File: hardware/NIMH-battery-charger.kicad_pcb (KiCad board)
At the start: 2 copper layers, 66 x 79.8 mm, 27 parts, among them J1 Conn_01x03_Pin, J3 Conn_01x01_Pin, J4 Conn_01x01_Pin, J5 Conn_01x01_Pin, J6 Conn_01x01_Pin, J7 USB_C_Receptacle_PowerOnly_6P, U1 CH32V003f4u6

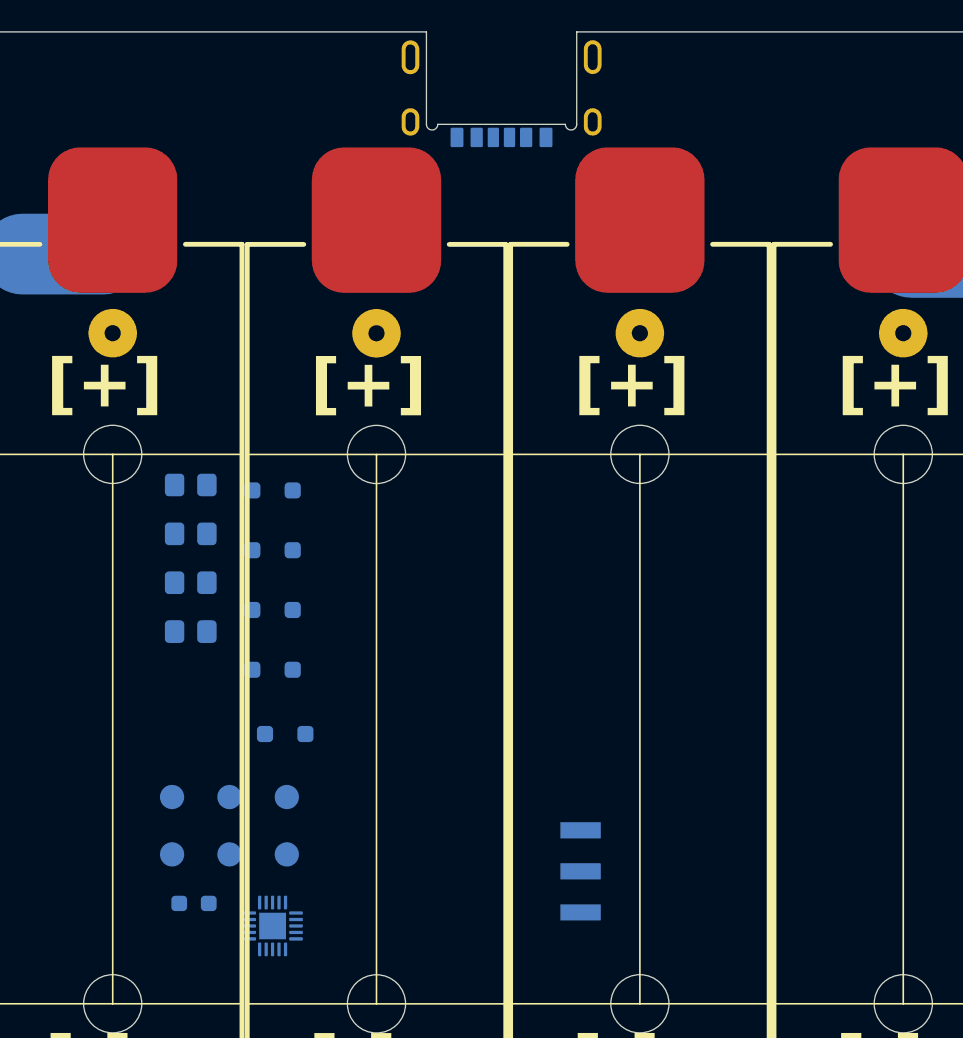
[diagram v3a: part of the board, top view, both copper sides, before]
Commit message: Add leds
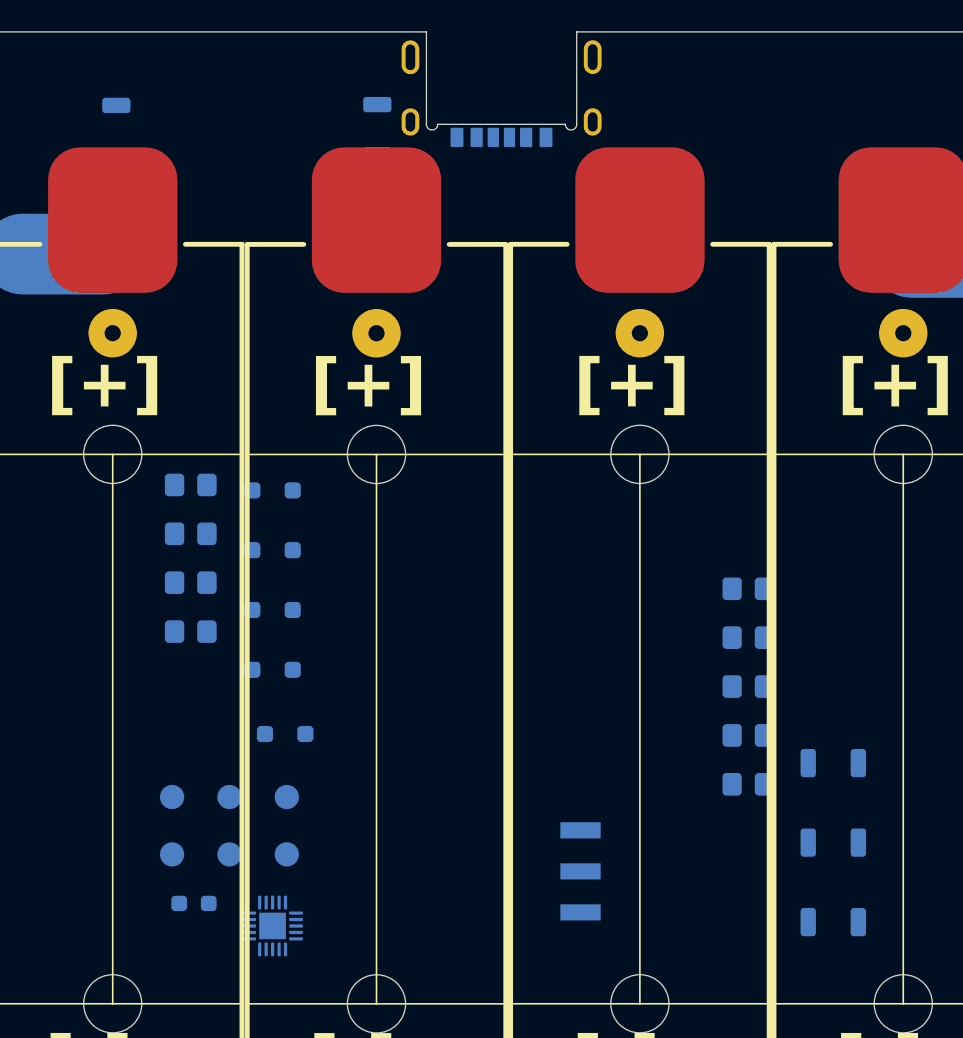
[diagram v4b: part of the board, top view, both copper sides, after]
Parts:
- added D10: LED, PCM_LED_SMD_AKL:LED_1206_3216Metric_ReverseMount_Hole1.8x2.4mm, B.Cu at (157.7, 99.1)
- added D5: LED, PCM_LED_SMD_AKL:LED_1206_3216Metric_ReverseMount_Hole1.8x2.4mm, B.Cu at (113.3, 50.1)
- added D6: LED, PCM_LED_SMD_AKL:LED_1206_3216Metric_ReverseMount_Hole1.8x2.4mm, B.Cu at (129.4, 50.1)
- added D7: LED, PCM_LED_SMD_AKL:LED_1206_3216Metric_ReverseMount_Hole1.8x2.4mm, B.Cu at (157.7, 89.3)
- added D8: LED, PCM_LED_SMD_AKL:LED_1206_3216Metric_ReverseMount_Hole1.8x2.4mm, B.Cu at (157.7, 94.2)
- added R10: 220R, PCM_Resistor_SMD_AKL:R_0805_2012Metric_Pad1.20x1.40mm_HandSolder, B.Cu at (152.4, 90.6)
- added R6: 220R, PCM_Resistor_SMD_AKL:R_0805_2012Metric_Pad1.20x1.40mm_HandSolder, B.Cu at (152.4, 78.5)
- added R7: 220R, PCM_Resistor_SMD_AKL:R_0805_2012Metric_Pad1.20x1.40mm_HandSolder, B.Cu at (152.4, 81.5)
- added R8: 220R, PCM_Resistor_SMD_AKL:R_0805_2012Metric_Pad1.20x1.40mm_HandSolder, B.Cu at (152.4, 84.6)
- added R9: 220R, PCM_Resistor_SMD_AKL:R_0805_2012Metric_Pad1.20x1.40mm_HandSolder, B.Cu at (152.4, 87.6)

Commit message: Moving Leds
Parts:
- moved D7 40.0 mm to (137.2, 54.9), turned to 90 degrees
- moved R6 0.09 mm to (152.5, 78.5)
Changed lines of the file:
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@@
 	(footprint "PCM_LED_SMD_AKL:LED_1206_3216Metric_ReverseMount_Hole1.8x2.4mm"
 		(layer "B.Cu")
-		(at 157.669668 89.3 180)
+		(at 137.25 54.85 90)
 		(descr "LED SMD 1206 (3216 Metric), reverse mount, square (rectangular) end terminal, IPC_7351 nominal, (Body size source: http://www.tortai-tech.com/upload/download/2011102023233369053.pdf), generated with kicad-footprint-generator")
 		(tags "diode reverse")
 		(property "Reference" "D7"
-			(at 0 2.545 0)
+			(at 0 2.545 90)
 			(layer "B.SilkS")
 			(effects
@@
 		)
 		(property "Value" "LED"
-			(at 0 -2.145 0)
+			(at 0 -2.145 90)
 			(layer "B.Fab")
 			(hide yes)
@@
 		)
 		(property "Footprint" "PCM_LED_SMD_AKL:LED_1206_3216Metric_ReverseMount_Hole1.8x2.4mm"
-			(at 0 0 0)
+			(at 0 0 90)
 			(layer "B.Fab")
 			(hide yes)
@@
 		)
 		(property "Datasheet" ""
-			(at 0 0 0)
+			(at 0 0 90)
 			(layer "B.Fab")
 			(hide yes)
@@
 		)
 		(property "Description" "Light emitting diode"
-			(at 0 0 0)
+			(at 0 0 90)
 			(layer "B.Fab")
 			(hide yes)
@@
 		(attr smd)
 		(fp_rect
-			(start -1.9 1.9)
-			(end -0.9 1.5)
-			(stroke
-				(width 0.12)
-				(type solid)
-			)
-			(fill solid)
-			(layer "B.SilkS")
-		)
-		(fp_rect
 			(start -1.9 -1.5)
 			(end -0.9 -1.9)
@@
 			(layer "B.SilkS")
 		)
+		(fp_rect
+			(start -1.9 1.9)
+			(end -0.9 1.5)
+			(stroke
+				(width 0.12)
+				(type solid)
+			)
+			(fill solid)
+			(layer "B.SilkS")
+		)
+		(fp_line
+			(start 2.28 -1.46)
+			(end 2.28 1.46)
+			(stroke
+				(width 0.05)
+				(type solid)
+			)
+			(layer "B.CrtYd")
+		)
+		(fp_line
+			(start -2.28 -1.46)
+			(end 2.28 -1.46)
+			(stroke
+				(width 0.05)
+				(type solid)
+			)
+			(layer "B.CrtYd")
+		)
 		(fp_line
 			(start 2.28 1.46)
@@
 		)
 		(fp_line
-			(start 2.28 -1.46)
-			(end 2.28 1.46)
-			(stroke
-				(width 0.05)
-				(type solid)
-			)
-			(layer "B.CrtYd")
-		)
-		(fp_line
 			(start -2.28 1.46)
 			(end -2.28 -1.46)
@@
 		)
 		(fp_line
-			(start -2.28 -1.46)
-			(end 2.28 -1.46)
-			(stroke
-				(width 0.05)
-				(type solid)
-			)
-			(layer "B.CrtYd")
+			(start 1.6 -0.8)
+			(end -1.6 -0.8)
+			(stroke
+				(width 0.1)
+				(type solid)
+			)
+			(layer "B.Fab")
+		)
+		(fp_line
+			(start -1.6 -0.8)
+			(end -1.6 0.8)
+			(stroke
+				(width 0.1)
+				(type solid)
+			)
+			(layer "B.Fab")
+		)
+		(fp_line
+			(start 0.6 -0.6)
+			(end 0.6 0.6)
+			(stroke
+				(width 0.1)
+				(type default)
+			)
+			(layer "B.Fab")
+		)
+		(fp_line
+			(start -0.6 -0.6)
+			(end -0.6 0.6)
+			(stroke
+				(width 0.1)
+				(type default)
+			)
+			(layer "B.Fab")
+		)
+		(fp_line
+			(start 1.3 0)
+			(end -1.3 0)
+			(stroke
+				(width 0.1)
+				(type default)
+			)
+			(layer "B.Fab")
+		)
+		(fp_line
+			(start -0.6 0)
+			(end 0.6 -0.6)
+			(stroke
+				(width 0.1)
+				(type default)
+			)
+			(layer "B.Fab")
+		)
+		(fp_line
+			(start 0.6 0.6)
+			(end -0.6 0)
+			(stroke
+				(width 0.1)
+				(type default)
+			)
+			(layer "B.Fab")
 		)
 		(fp_line
@@
 		)
 		(fp_line
-			(start 1.6 -0.8)
-			(end -1.6 -0.8)
-			(stroke
-				(width 0.1)
-				(type solid)
-			)
-			(layer "B.Fab")
-		)
-		(fp_line
-			(start 1.3 0)
-			(end -1.3 0)
-			(stroke
-				(width 0.1)
-				(type default)
-			)
-			(layer "B.Fab")
-		)
-		(fp_line
-			(start 0.6 0.6)
-			(end -0.6 0)
-			(stroke
-				(width 0.1)
-				(type default)
-			)
-			(layer "B.Fab")
-		)
-		(fp_line
-			(start 0.6 -0.6)
-			(end 0.6 0.6)
-			(stroke
-				(width 0.1)
-				(type default)
-			)
-			(layer "B.Fab")
-		)
-		(fp_line
-			(start -0.6 0)
-			(end 0.6 -0.6)
-			(stroke
-				(width 0.1)
-				(type default)
-			)
-			(layer "B.Fab")
-		)
-		(fp_line
-			(start -0.6 -0.6)
-			(end -0.6 0.6)
-			(stroke
-				(width 0.1)
-				(type default)
-			)
-			(layer "B.Fab")
-		)
-		(fp_line
 			(start -1.6 0.8)
 			(end 1.6 0.8)
@@
 			(layer "B.Fab")
 		)
-		(fp_line
-			(start -1.6 -0.8)
-			(end -1.6 0.8)
-			(stroke
-				(width 0.1)
-				(type solid)
-			)
-			(layer "B.Fab")
-		)
 		(fp_text user "${REFERENCE}"
-			(at 0 1.4 0)
+			(at 0 1.4 90)
 			(layer "B.Fab")
 			(effects
@@
 		)
 		(pad "" np_thru_hole oval
-			(at 0 0 180)
+			(at 0 0 90)
 			(size 1.8 2.4)
 			(drill oval 1.8 2.4)
@@
 		)
 		(pad "1" smd roundrect
-			(at -1.55 0 180)
+			(at -1.55 0 90)
 			(size 0.95 1.75)
 			(layers "B.Cu" "B.Paste" "B.Mask")
@@
 		)
 		(pad "2" smd roundrect
-			(at 1.55 0 180)
+			(at 1.55 0 90)
 			(size 0.95 1.75)
 			(layers "B.Cu" "B.Paste" "B.Mask")
@@
 	(footprint "PCM_Resistor_SMD_AKL:R_0805_2012Metric_Pad1.20x1.40mm_HandSolder"
 		(layer "B.Cu")
-		(at 152.408168 78.5125 180)
+		(at 152.5 78.5125 180)
 		(descr "Resistor SMD 0805 (2012 Metric), square (rectangular) end terminal, IPC_7351 nominal with elongated pad for handsoldering. (Body size source: IPC-SM-782 page 72, https://www.pcb-3d.com/wordpress/wp-content/uploads/ipc-sm-782a_amendment_1_and_2.pdf), Alternate KiCad Library")
 		(tags "resistor handsolder")

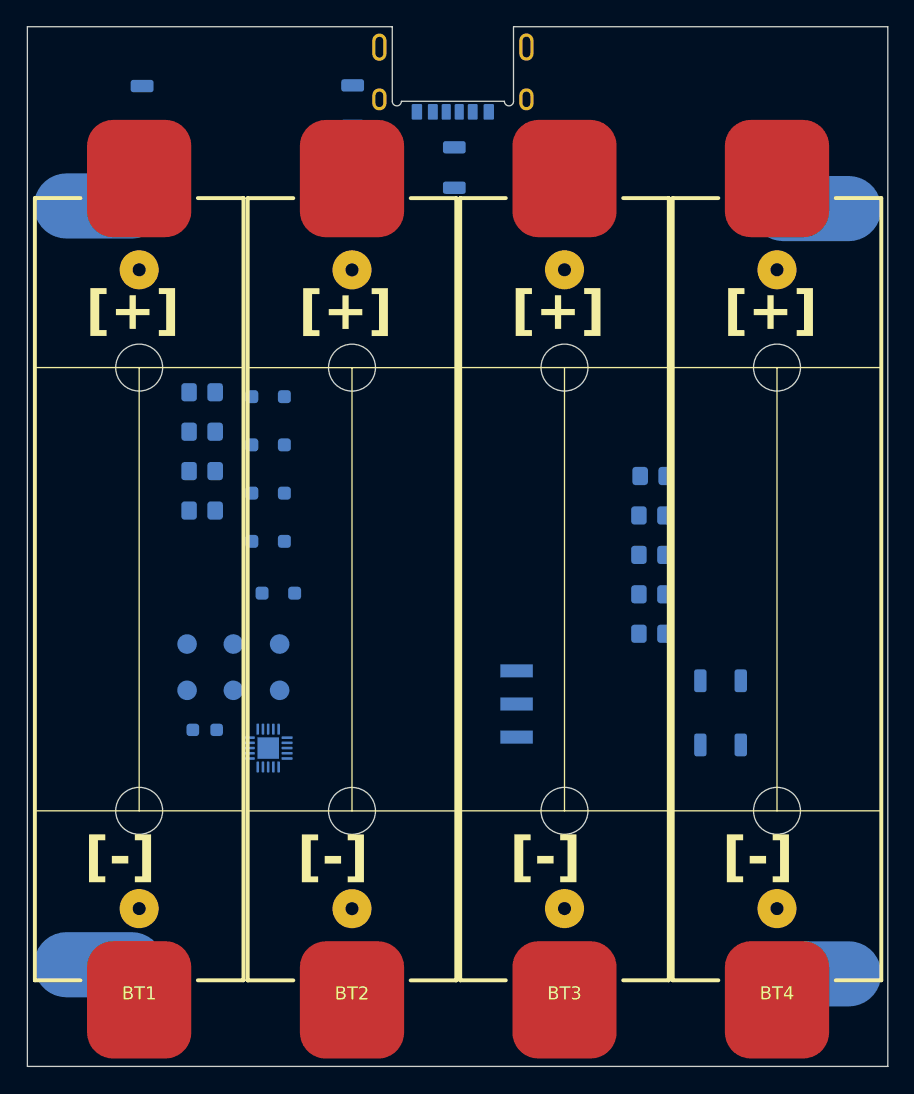
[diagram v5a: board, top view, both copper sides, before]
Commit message: Placed all components on board
Finalizing PCB
Add all components and place them for routing
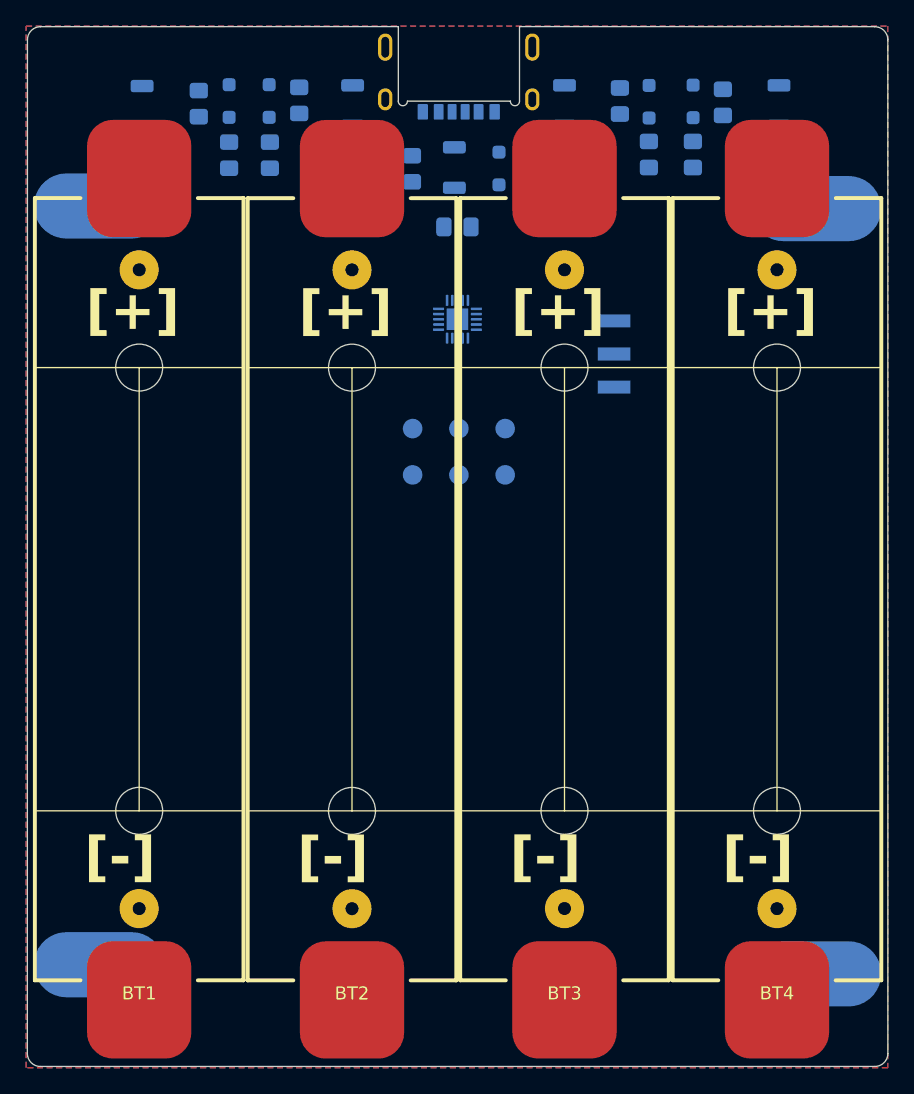
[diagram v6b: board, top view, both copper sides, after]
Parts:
- added C1: 100n, PCM_Capacitor_SMD_AKL:C_0805_2012Metric_Pad1.18x1.45mm, B.Cu at (137.5, 59.4)
- added C2: 100n, PCM_Capacitor_SMD_AKL:C_0805_2012Metric_Pad1.18x1.45mm, B.Cu at (143.6, 54.9)
- moved D10 49.2 mm to (162.2, 50.1), turned to 90 degrees
- moved D4 46.9 mm to (155.6, 49.8), turned to 90 degrees
- moved R5 46.5 mm to (155.6, 53.9), turned to -90 degrees
- moved D8 45.7 mm to (145.7, 50.1), turned to 90 degrees
- moved R6 45.1 mm to (117.7, 50.0), turned to 90 degrees
- moved R3 45.0 mm to (131.5, 55.0), turned to -90 degrees
- moved R4 42.0 mm to (152.2, 53.9), turned to -90 degrees
- moved D3 41.9 mm to (152.2, 49.8), turned to 90 degrees
- moved R7 41.8 mm to (125.3, 49.7), turned to 90 degrees
- moved R10 41.1 mm to (157.8, 49.9), turned to 90 degrees
- moved R9 37.9 mm to (149.9, 49.8), turned to 90 degrees
- moved D9 36.7 mm to (140.7, 54.9), turned to 90 degrees
- moved U1 36.0 mm to (137.5, 66.5), turned to -90 degrees
- moved R8 34.9 mm to (134.0, 55.0), turned to -90 degrees
- moved J1 32.6 mm to (155.0, 69.2), turned to 0 degrees
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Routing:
- added copper zone on B.Cu, net GND
- added copper zone on F.Cu, net GND
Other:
- outline, holes or cut-outs redrawn

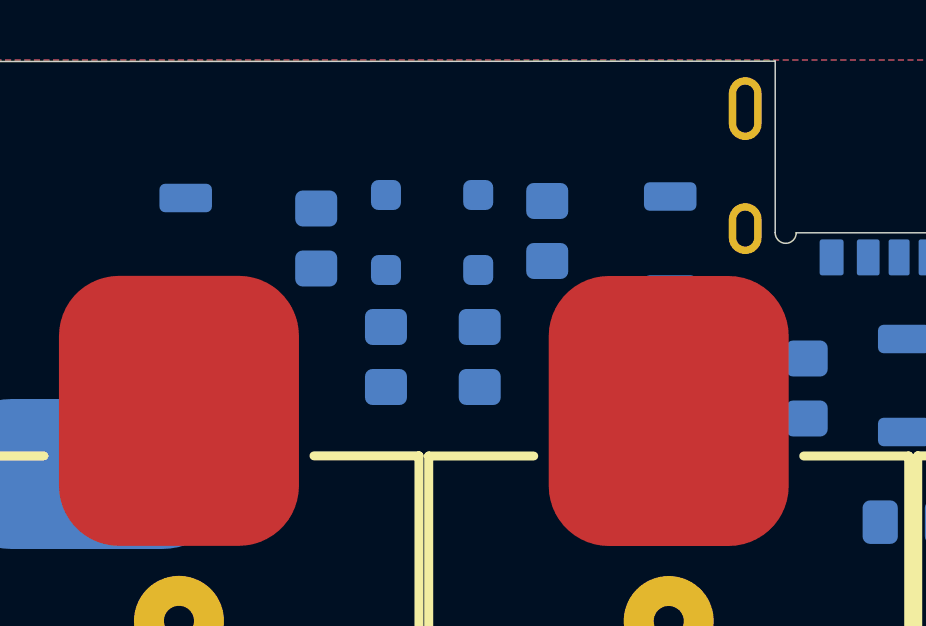
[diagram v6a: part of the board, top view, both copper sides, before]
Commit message: Adding soild GND connection to some pins of USB connector
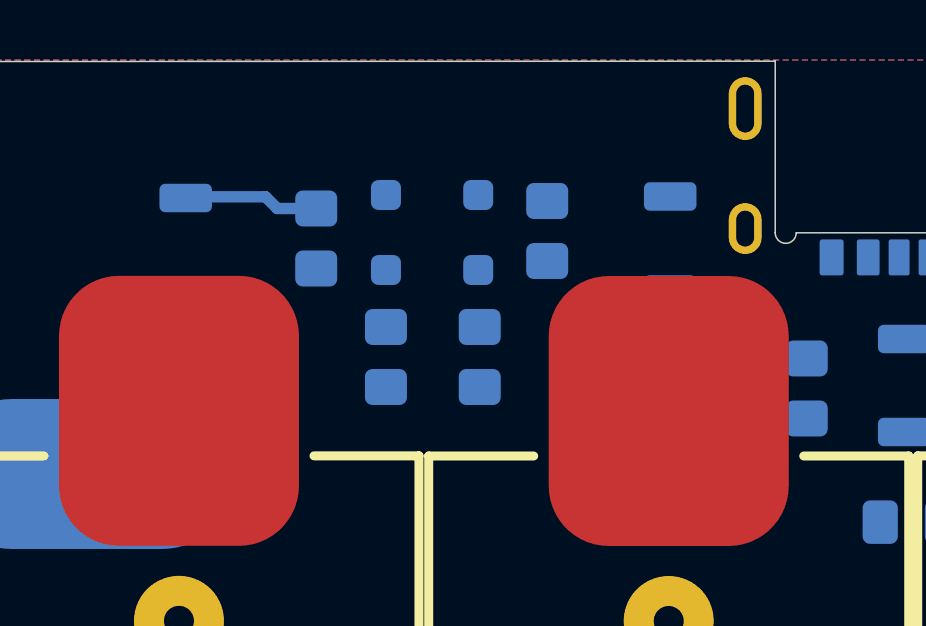
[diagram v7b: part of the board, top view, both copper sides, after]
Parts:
- removed R3: 0R, PCM_Resistor_SMD_AKL:R_0603_1608Metric_Pad0.98x0.95mm_HandSolder
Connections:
- J7 pad S1: Net-(J7-SHIELD) -> GND
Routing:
- net Net-(D5-A): track 0.00 -> 4.51 mm
